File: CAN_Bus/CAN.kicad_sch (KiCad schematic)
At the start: 13 parts, among them SW1 SW_Slide_DPDT, SW2 SW_SPST, U1 MCP2515-xSO, U2 MCP2561-E-P, Y1 8MHz, Y2 16MHz

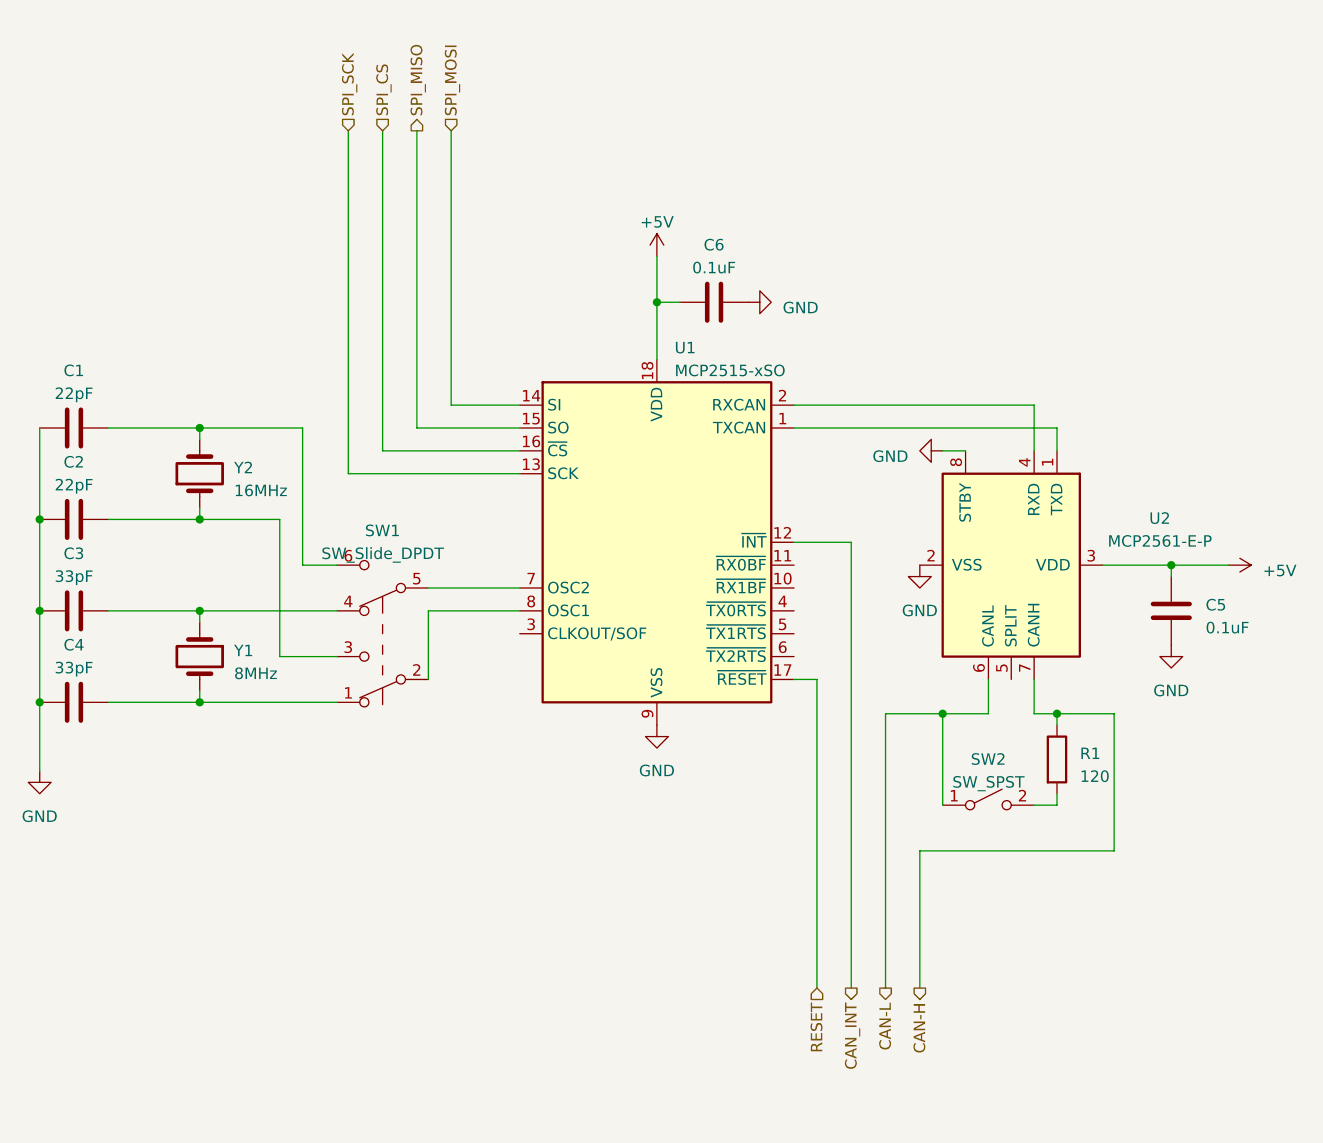
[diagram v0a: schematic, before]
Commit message: finalized schematic (not pcb)
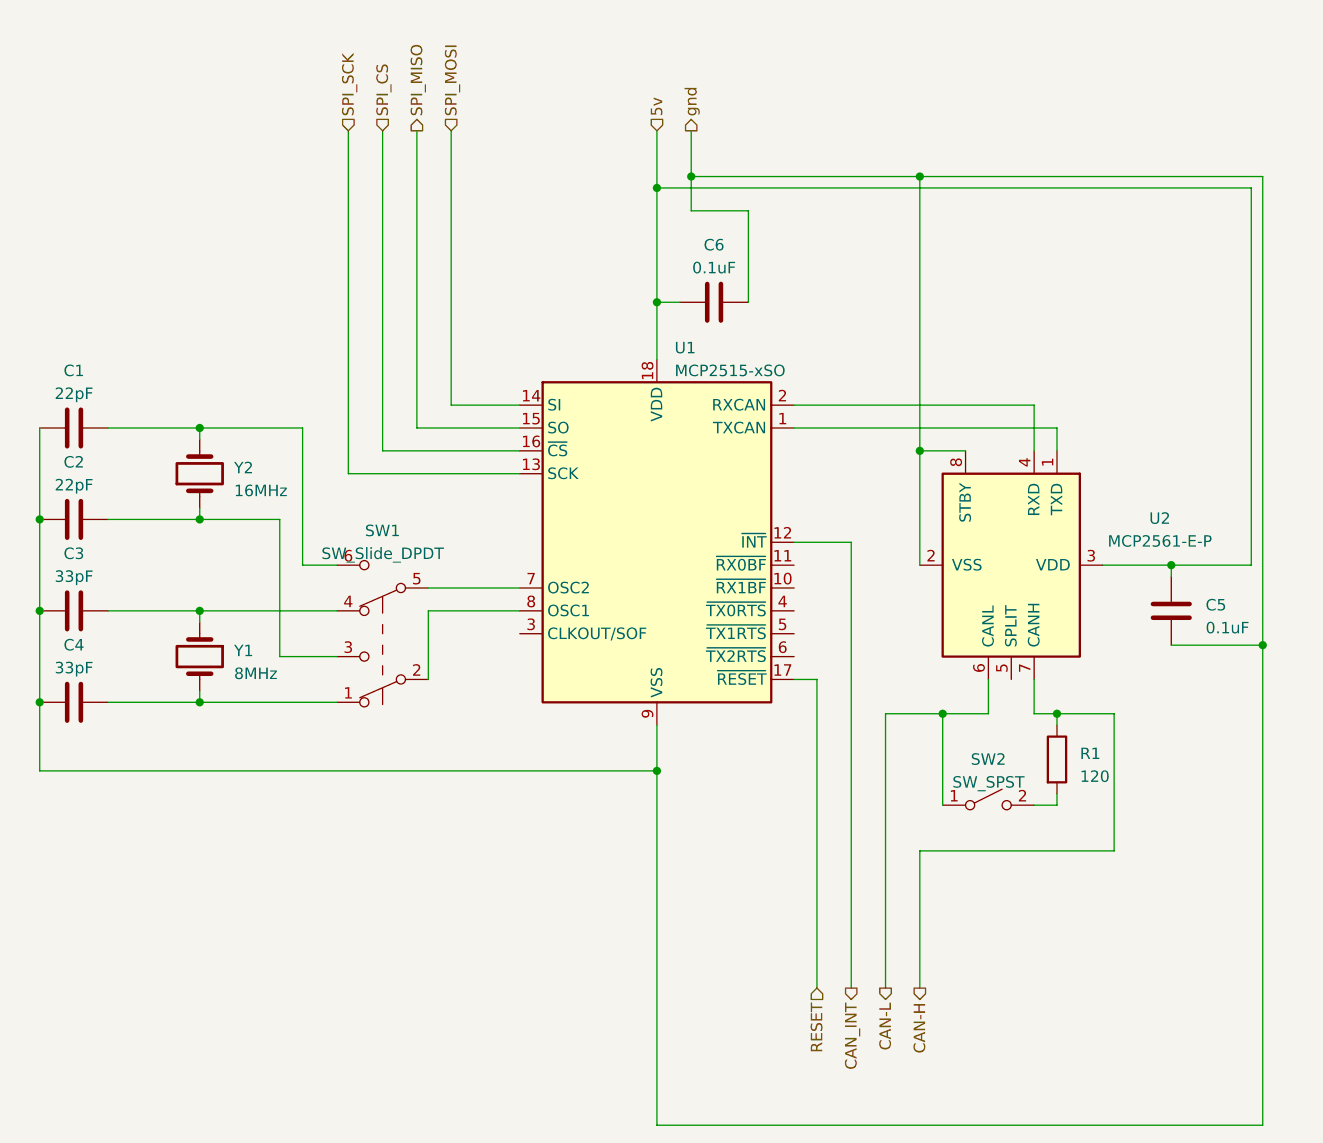
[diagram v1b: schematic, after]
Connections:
- net +5V renamed 5v
- net GND renamed gnd
